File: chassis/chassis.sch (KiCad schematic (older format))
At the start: 27 parts, among them J1 MicroD-15Pins, J10 MicroD-37Pins, J2 MicroD-15Pins, J200 Conn_01x04, J202 Conn_01x07, J203 MilSpec-91Pins, J3 MicroD-37Pins, J4 MicroD-37Pins, J5 MicroD-37Pins, J6 MicroD-37Pins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

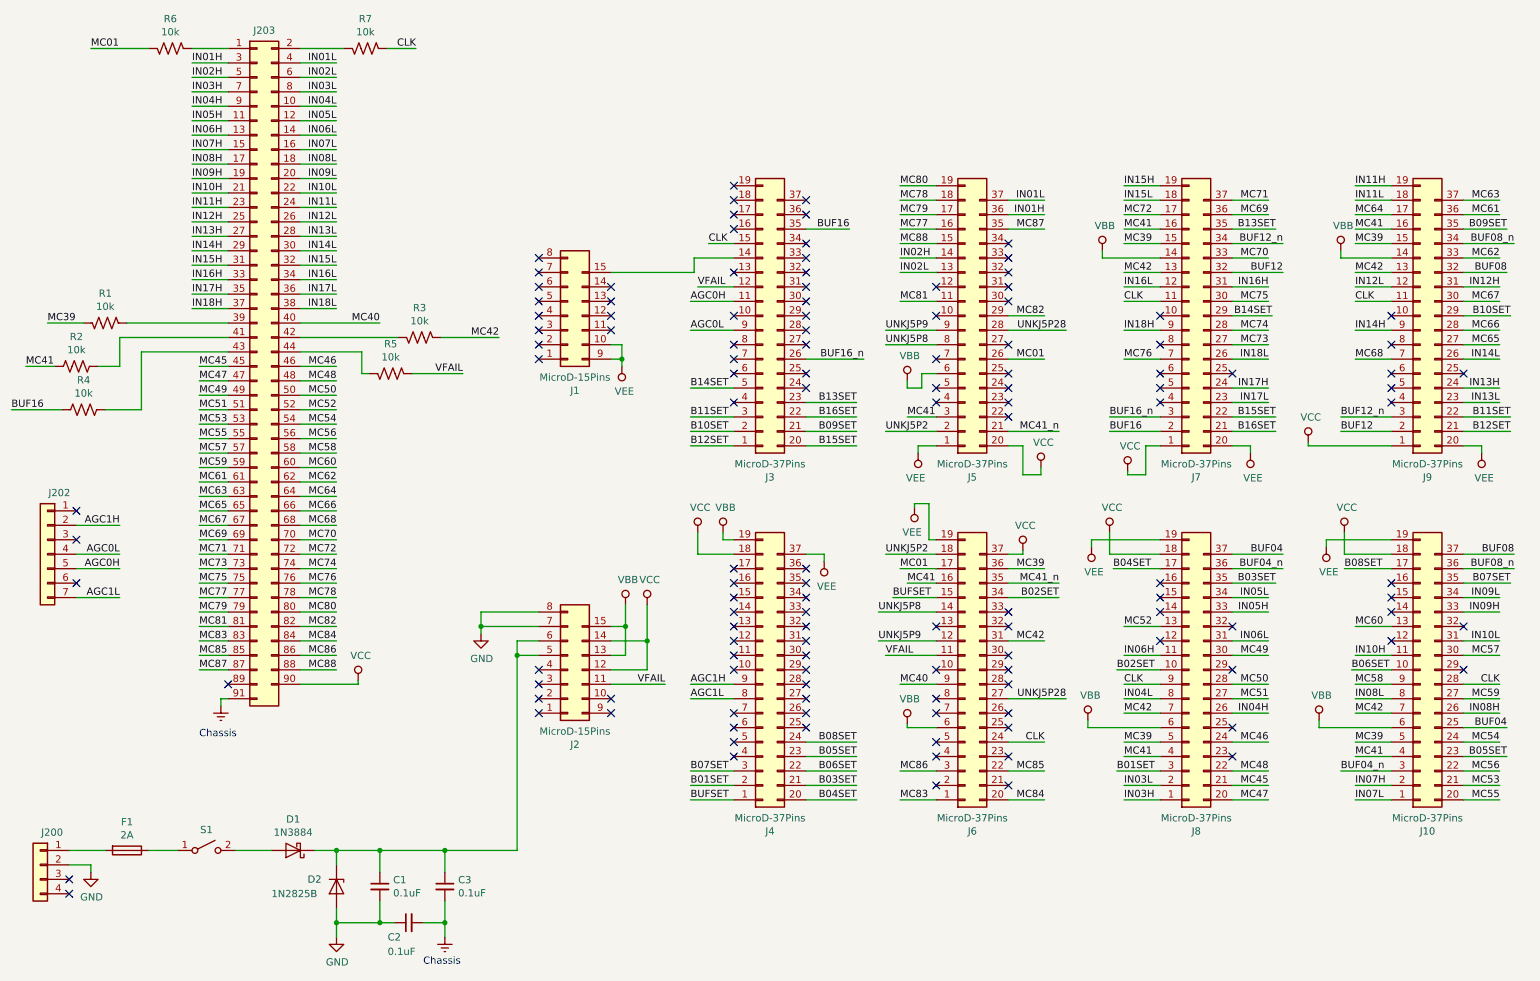
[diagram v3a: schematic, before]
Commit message: Finished untangling the module 3 schematics and gave every net a name
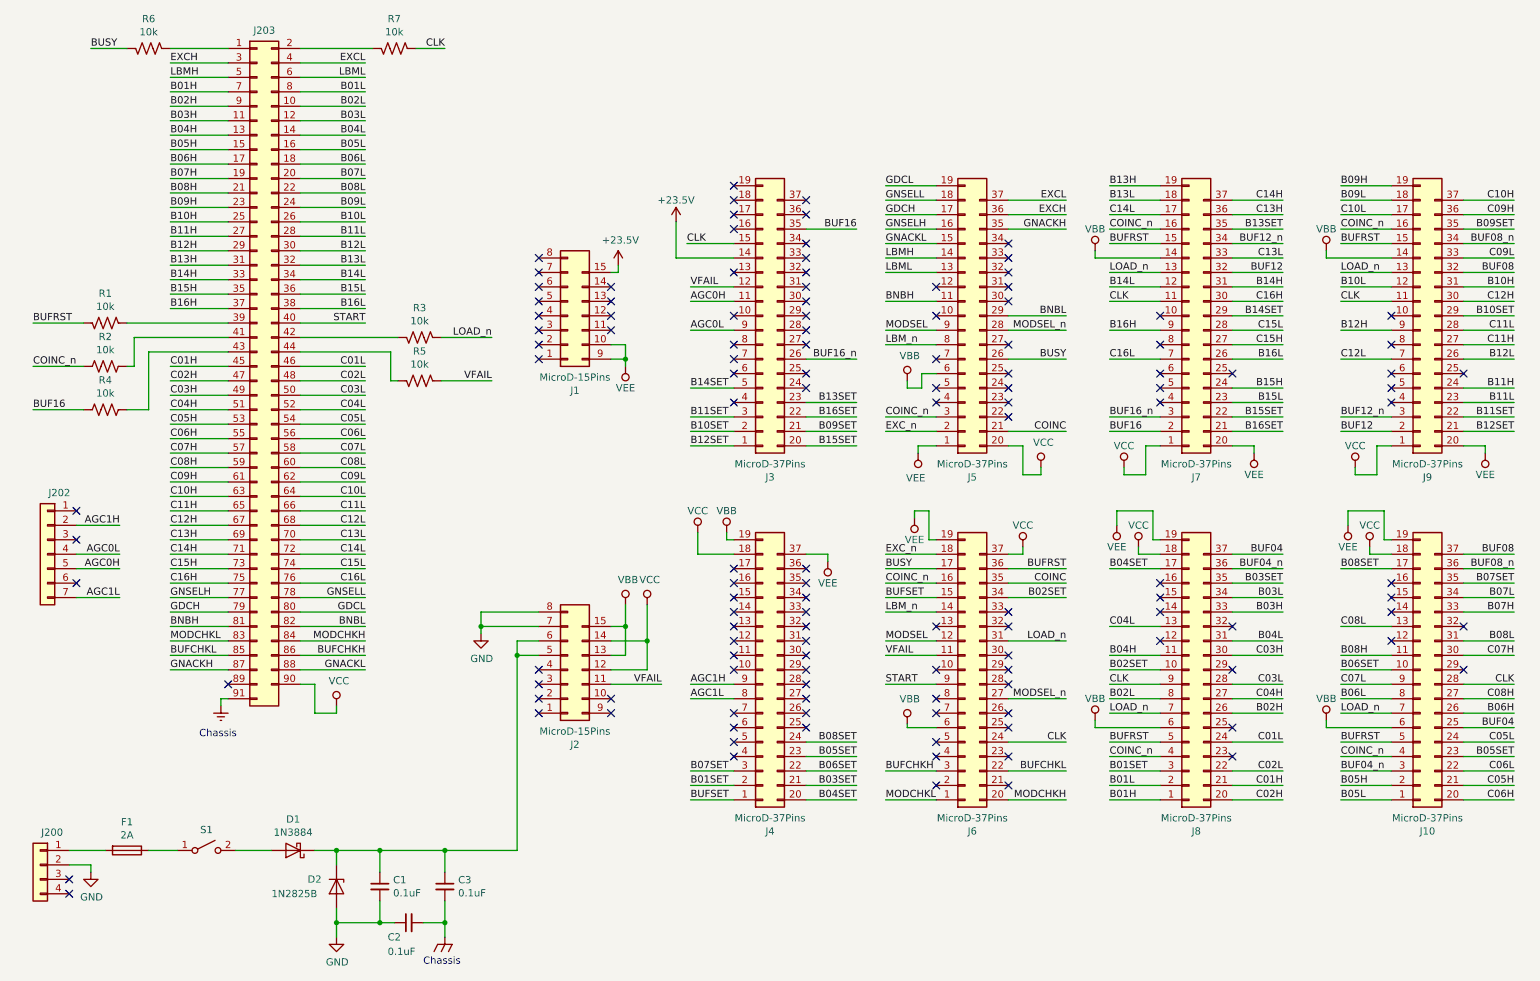
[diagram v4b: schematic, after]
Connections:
- net Earth: no longer C2.2, C3.2
- net +24V: now reaches J1.15 (Pin_15), J3.14 (Pin_14)
- net IN01H renamed EXCH
- net IN01L renamed EXCL
- net IN02H renamed LBMH
- net IN02L renamed LBML
- net IN03H renamed B01H
- net IN03L renamed B01L
- net IN04H renamed B02H
- net IN04L renamed B02L
- net IN05H renamed B03H
- net IN05L renamed B03L
- net IN06H renamed B04H
- net IN06L renamed B04L
- net IN07H renamed B05H
- net IN07L renamed B05L
- net IN08H renamed B06H
- net IN08L renamed B06L
- net IN09H renamed B07H
- net IN09L renamed B07L
- net IN10H renamed B08H
- net IN10L renamed B08L
- net IN11H renamed B09H
- net IN11L renamed B09L
- net IN12H renamed B10H
- net IN12L renamed B10L
- net IN13H renamed B11H
- net IN13L renamed B11L
- net IN14H renamed B12H
- net IN14L renamed B12L
- net IN15H renamed B13H
- net IN15L renamed B13L
- net IN16H renamed B14H
- net IN16L renamed B14L
- net IN17H renamed B15H
- net IN17L renamed B15L
- net IN18H renamed B16H
- net IN18L renamed B16L
- net MC01 renamed BUSY
- net MC39 renamed BUFRST
- net MC40 renamed START
- net MC41 renamed COINC_n
- net MC41_n renamed COINC
- net MC42 renamed LOAD_n
- net MC45 renamed C01H
- net MC46 renamed C01L
- net MC47 renamed C02H
- net MC48 renamed C02L
- net MC49 renamed C03H
- net MC50 renamed C03L
- net MC51 renamed C04H
- net MC52 renamed C04L
- net MC53 renamed C05H
- net MC54 renamed C05L
- net MC55 renamed C06H
- net MC56 renamed C06L
- net MC57 renamed C07H
- net MC58 renamed C07L
- net MC59 renamed C08H
- net MC60 renamed C08L
- net MC61 renamed C09H
- net MC62 renamed C09L
- net MC63 renamed C10H
- net MC64 renamed C10L
- net MC65 renamed C11H
- net MC66 renamed C11L
- net MC67 renamed C12H
- net MC68 renamed C12L
- net MC69 renamed C13H
- net MC70 renamed C13L
- net MC71 renamed C14H
- net MC72 renamed C14L
- net MC73 renamed C15H
- net MC74 renamed C15L
- net MC75 renamed C16H
- net MC76 renamed C16L
- net MC77 renamed GNSELH
- net MC78 renamed GNSELL
- net MC79 renamed GDCH
- net MC80 renamed GDCL
- net MC81 renamed BNBH
- net MC82 renamed BNBL
- net MC83 renamed MODCHKL
- net MC84 renamed MODCHKH
- net MC85 renamed BUFCHKL
- net MC86 renamed BUFCHKH
- net MC87 renamed GNACKH
- net MC88 renamed GNACKL
- net UNKJ5P2 renamed EXC_n
- net UNKJ5P28 renamed MODSEL_n
- net UNKJ5P8 renamed LBM_n
- net UNKJ5P9 renamed MODSEL
- new net Chassis: C2.2, C3.2
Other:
- moved on the sheet: R2, R4, R5, R6, R7

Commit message: Added a schematic for module 4 board 2, which has two small differences from the other three four-bit modules. Also fixed a pinout error on module 5 board 2.
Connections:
- net B05H: now also J10.1 (Pin_1); no longer J10.2 (Pin_2)
- net B05L: now also J10.2 (Pin_2); no longer J10.1 (Pin_1)
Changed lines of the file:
@@
 Wire Wire Line
 	10200 6000 9850 6000
-Text Label 9850 6000 0    50   ~ 0
+Text Label 9850 5900 0    50   ~ 0
 B05L
 Wire Wire Line
 	10200 5900 9850 5900
-Text Label 9850 5900 0    50   ~ 0
+Text Label 9850 6000 0    50   ~ 0
 B05H
 Wire Wire Line
